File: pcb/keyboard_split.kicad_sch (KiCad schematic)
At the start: 69 parts, among them J1 JST_ACH_BM02B-ACHSS-GAN-ETF_P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, J2 JST_ACH_BM02B-ACHSS-GAN-ETF_S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, SW1 CPG135001S30, SW10 CPG135001S30, SW11 CPG135001S30, SW12 CPG135001S30, SW13 CPG135001S30, SW14 CPG135001S30, SW15 CPG135001S30, SW16 CPG135001S30, SW17 CPG135001S30, SW18 CPG135001S30, SW19 CPG135001S30, SW2 CPG135001S30, SW20 CPG135001S30, SW21 CPG135001S30, SW22 CPG135001S30, SW23 CPG135001S30, SW24 CPG135001S30, SW25 CPG135001S30, SW26 CPG135001S30, SW27 CPG135001S30, SW28 CPG135001S30, SW29 CPG135001S30, SW3 CPG135001S30, SW30 RotaryEncoder_Switch, SW4 CPG135001S30, SW5 CPG135001S30, SW6 CPG135001S30, SW7 CPG135001S30, SW8 CPG135001S30, SW9 CPG135001S30, U1 nice!nano v2

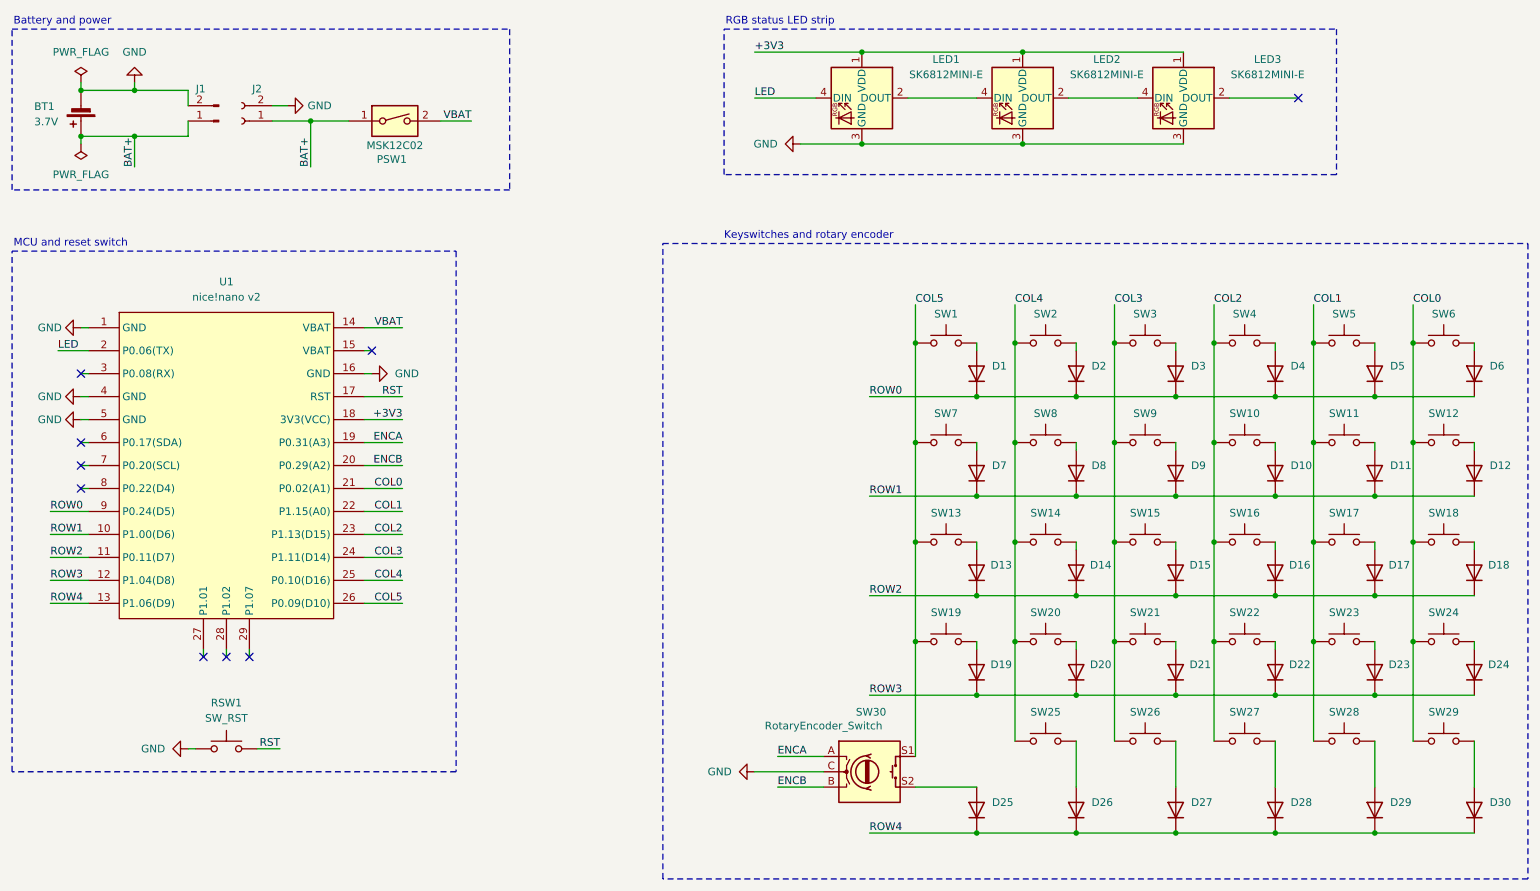
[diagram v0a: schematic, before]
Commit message: Correct schematic reference numbering.
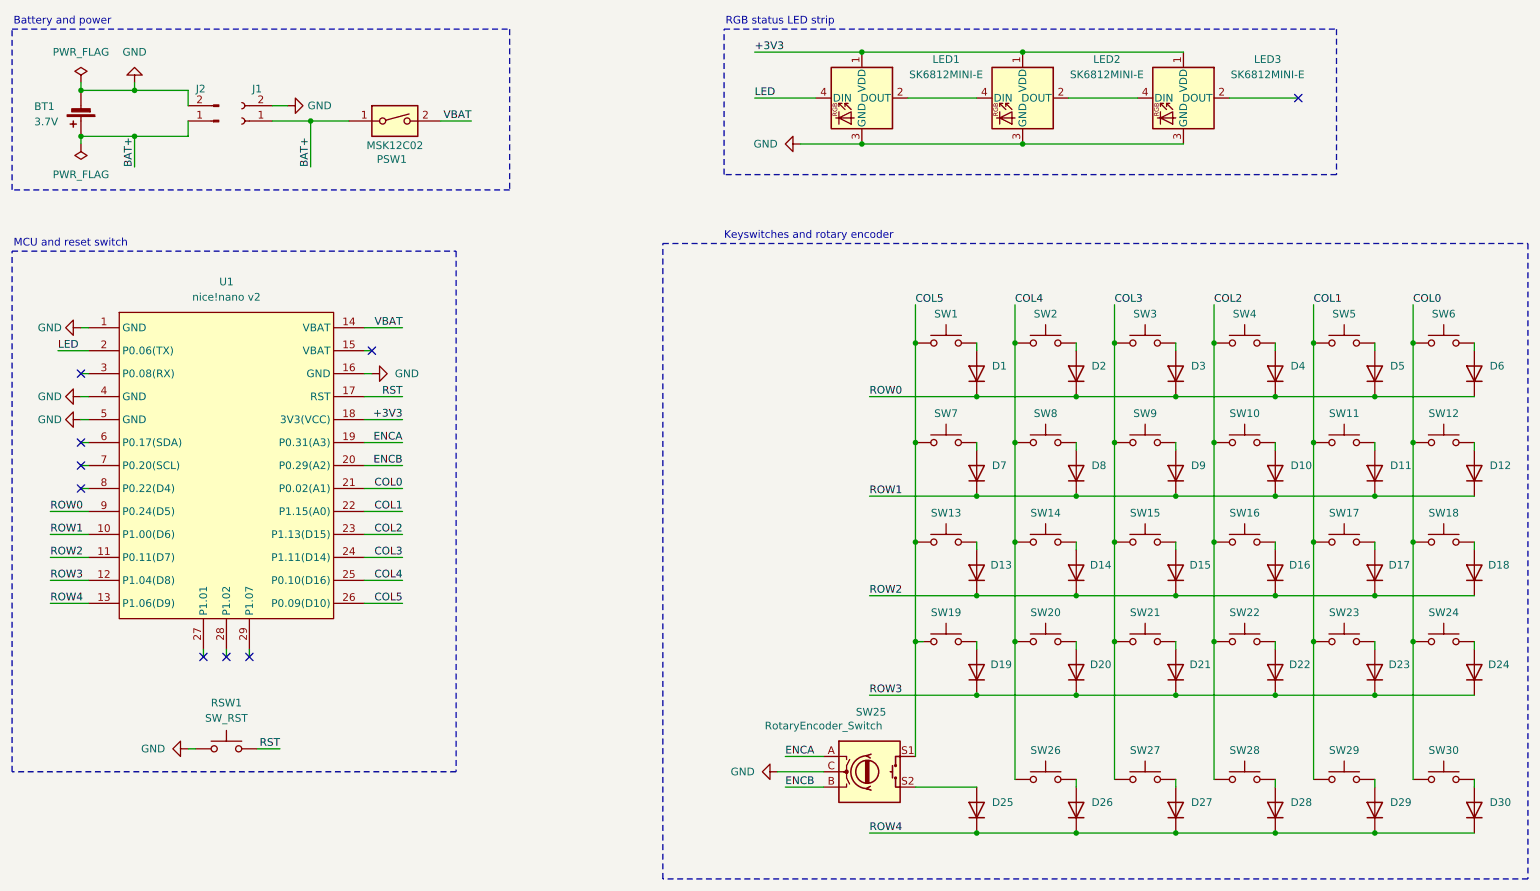
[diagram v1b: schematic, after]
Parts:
- renumbered J2 to J1, J1 to J2, SW30 to SW25, SW25 to SW26, SW26 to SW27, SW27 to SW28, SW28 to SW29, SW29 to SW30
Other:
- moved on the sheet: SW26, SW27, SW28, SW29, SW30
